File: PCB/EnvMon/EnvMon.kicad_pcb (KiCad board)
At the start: 2 copper layers, 57.5 x 37 mm, 37 parts, among them J1 USB-C, J2 DC, J3 TEMP, J5 Shelly, M1 OLED1.5-RGB, SW1 SW_Push, SW2 SW_Push, SW3 SW_Push, U1 ESP32-S3-MINI-1, U2 SCD41, U5 QR, U6 MD8942, U7 SHT40, U8 VEML6040

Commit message: WS2812B LED
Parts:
- removed D1: RGB, RevK:LED-RGB-1.6x1.6
- removed R1: 680R, RevK:R_0402
- removed R17: 220R, RevK:R_0402
- removed R2: 2K, RevK:R_0402
- added D4: XL-1010RGBC-WS2812B, RevK:SMD1010, F.Cu at (136.2, 64.8)
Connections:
- U1 pad 36: G -> unconnected-(U1-GPIO40-Pad36)
- U1 pad 37: R -> unconnected-(U1-GPIO41-Pad37)
- U1 pad 38: B -> unconnected-(U1-GPIO42-Pad38)
- U1 pad 41: unconnected-(U1-GPIO45-Pad41) -> LED
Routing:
- net G: track 13.7 -> 0.00 mm
- net LED: track 0.00 -> 13.5 mm
- net R: track 12.6 -> 0.00 mm
- net B: track 11.4 -> 0.00 mm
- net +3.3V: track 155.4 -> 159.2 mm
- net Net-(D1-RK): track 2.51 -> 0.00 mm
- net Net-(D1-GK): track 0.90 -> 0.00 mm
- net Net-(D1-BK): track 0.90 -> 0.00 mm
- net SCL: track 94.8 -> 94.2 mm
- added copper zone on B.Cu, net +3.3V
- added copper zone on F.Cu, net +3.3V

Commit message: Tidy
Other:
- board text added: "RGB:45"
- board text added: "SCL:38 SDA:39"
- board text removed: "RGB: 41/40/42"
- board text removed: "SCL: 38 SDA: 39"

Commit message: New
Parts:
- D2: value D -> Schottky; footprint RevK:D_SOD-123 -> RevK:D_1206

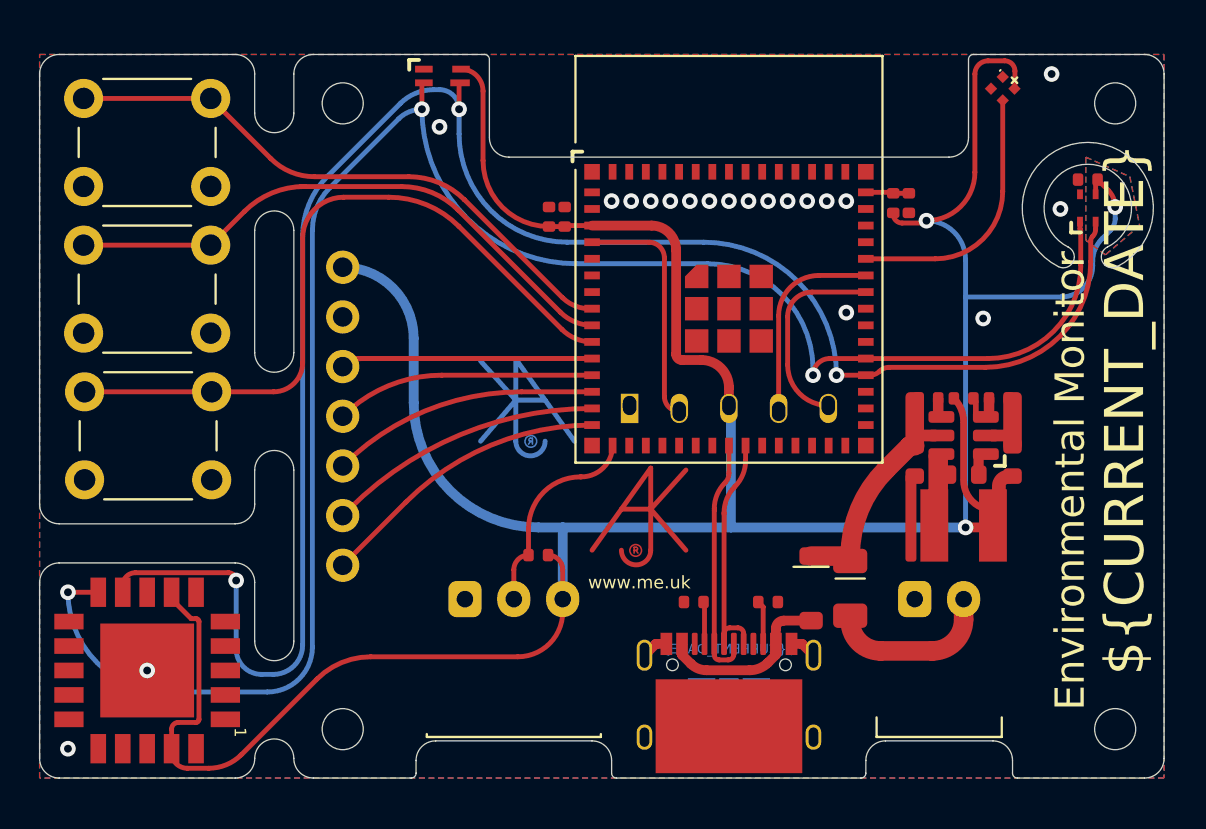
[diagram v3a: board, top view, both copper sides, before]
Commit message: New plugs
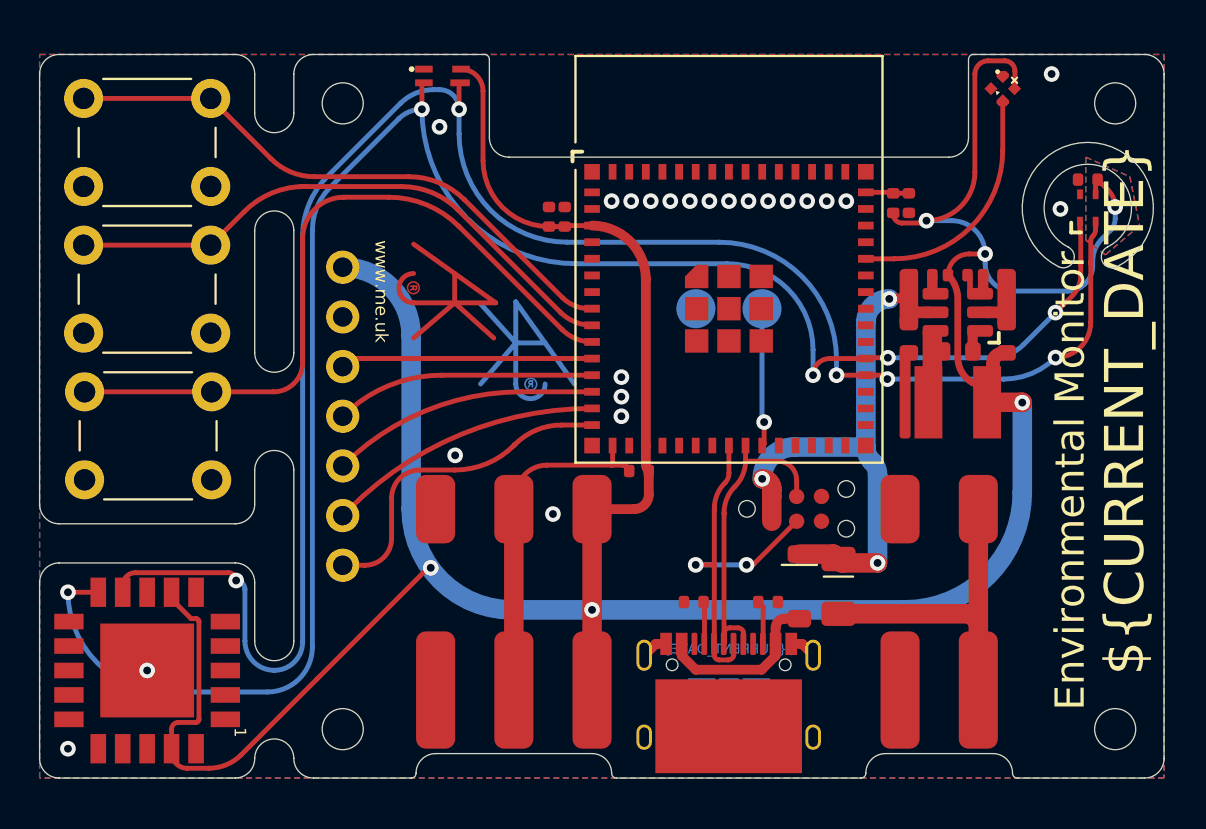
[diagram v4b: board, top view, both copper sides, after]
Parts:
- removed J1: USB-C, RevK:USC16-TR
- added J4: TC2030-USB-NL-DS, RevK:Tag-Connect_TC2030-IDC-NL_2x03_P1.27mm_Vertical, F.Cu at (125.7, 86.2)
- added J6: USB-C-Socket-V, RevK:USB-C-Socket-H, F.Cu at (122.2, 94.2)
- added REF**: Shadow, RevK:Shadow, F.Cu at (120.0, 80.0)
- J2: footprint RevK:PTSM-HH-2-RA-W -> RevK:WAGO-2060-452-998-404
- J3: footprint RevK:PTSM-HH-3-RA -> RevK:WAGO-2060-453-998-404
- J5: value Shelly -> Reset; footprint RevK:Shelly -> RevK:AA-Pad
- moved Logo2 14.6 mm to (108.2, 75.7), turned to -90 degrees
- moved R13 6.71 mm to (117.7, 84.3)
- moved C6 6.31 mm to (131.4, 77.5)
- moved C7 6.31 mm to (136.4, 77.5)
- moved C8 6.31 mm to (133.9, 78.2)
- moved L2 6.31 mm to (133.9, 80.8)
- moved R14 6.31 mm to (133.9, 74.3)
- moved R15 6.31 mm to (135.8, 74.3)
- moved U6 6.31 mm to (133.9, 76.2)
- moved R16 6.31 mm to (132.2, 74.3)
- moved J5 5.10 mm to (122.2, 76.0)
- moved Logo1 2.92 mm to (111.3, 77.8)
- moved D3 0.61 mm to (125.8, 90.2)
- moved D2 0.61 mm to (127.8, 90.2)
- turned J2 to 90 degrees
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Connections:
- J5 pad 2: Net-(J5-0) -> Net-(J5-Pin_2)
- U1 pad 18: unconnected-(U1-GPIO14-Pad18) -> +3.3V
- U1 pad 25: RX -> Net-(J5-Pin_2)
- U1 pad 27: TX -> unconnected-(U1-GPIO47-Pad27)
- U1 pad 39: Net-(J5-Tx) -> unconnected-(U1-GPIO43-Pad39)
- U1 pad 4: Net-(J5-0) -> unconnected-(U1-GPIO0-Pad4)
- U1 pad 40: Net-(J5-Rx) -> unconnected-(U1-GPIO44-Pad40)
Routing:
- net DC: track 8.85 -> 28.1 mm, vias 0 -> 3
- net Net-(J5-0): track 12.4 -> 0.00 mm
- net Net-(J5-Rx): track 10.4 -> 0.00 mm
- net Net-(J5-Tx): track 10.3 -> 0.00 mm
- net Net-(D2-A): track 8.52 -> 16.6 mm
- net TEMP: track 10.6 -> 17.7 mm
- net Net-(J5-Pin_2): track 0.00 -> 7.11 mm, vias 0 -> 1
- net D-: track 12.7 -> 19.7 mm, vias 0 -> 2
- net D+: track 12.8 -> 16.8 mm
- net OLED-RST: track 15.1 -> 16.9 mm
- net SCL: track 94.2 -> 95.6 mm, vias 3 -> 5
- net LED: track 13.5 -> 12.5 mm
- net SDA: track 95.7 -> 96.1 mm, vias 3 -> 5
- net +3.3V: track 159.2 -> 159.5 mm, vias 3 -> 6
- net GND: vias 20 -> 23
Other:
- outline, holes or cut-outs redrawn
- board text added: "21"

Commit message: PCB Update
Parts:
- J6: value USB-C-Socket-V -> USB-C-Socket-H
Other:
- copper layers 2 -> 4
